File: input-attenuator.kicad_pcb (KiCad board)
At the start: 2 copper layers, 90.2 x 57.7 mm, 90 parts, among them J1 DC_INTF, J2 DC_INTF, J3 RX_1_RF, J4 RX_2_RF, J5 RF_IN, K1 EE2-5TNU-L, K2 EE2-5TNU-L, K3 EE2-5TNU-L, K4 EE2-5TNU-L, Q1 BC858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

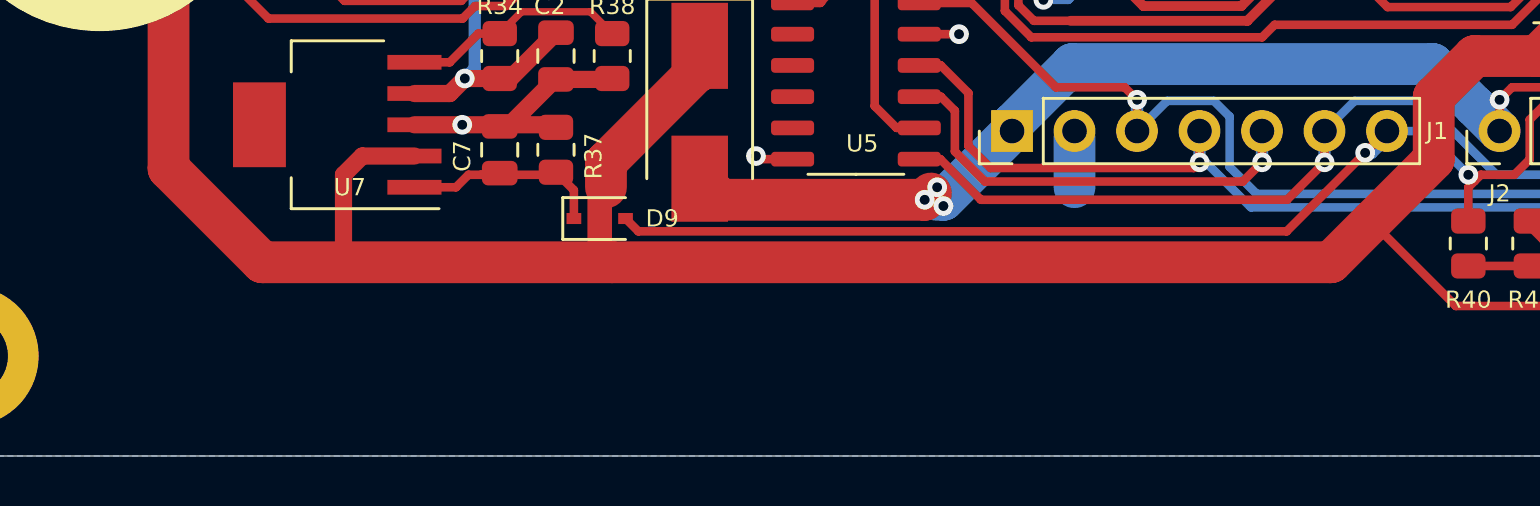
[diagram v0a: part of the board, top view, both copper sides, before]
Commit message: Updated layout with inrush resistor
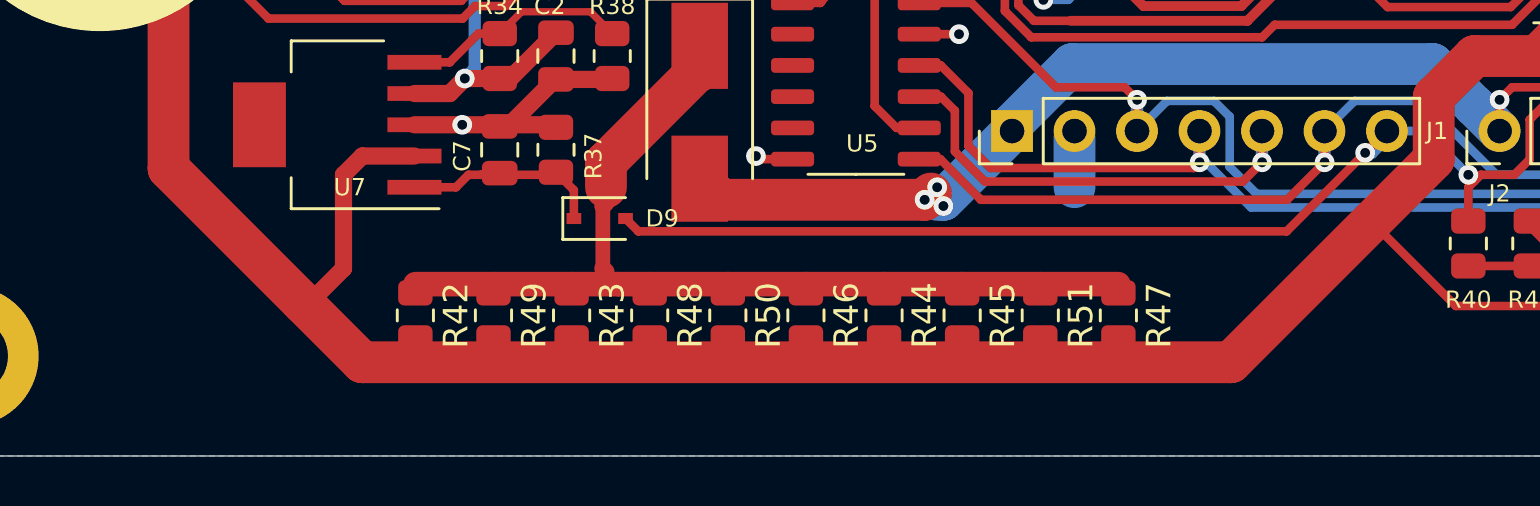
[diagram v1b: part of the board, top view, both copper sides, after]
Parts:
- added R42: 3K3, Resistor_SMD:R_0805_2012Metric, F.Cu at (85.7, 76.8)
- added R43: 3K3, Resistor_SMD:R_0805_2012Metric, F.Cu at (92.1, 76.8)
- added R44: 3K3, Resistor_SMD:R_0805_2012Metric, F.Cu at (104.8, 76.8)
- added R45: 3K3, Resistor_SMD:R_0805_2012Metric, F.Cu at (108.0, 76.8)
- added R46: 3K3, Resistor_SMD:R_0805_2012Metric, F.Cu at (101.6, 76.8)
- added R47: 3K3, Resistor_SMD:R_0805_2012Metric, F.Cu at (114.3, 76.8)
- added R48: 3K3, Resistor_SMD:R_0805_2012Metric, F.Cu at (95.2, 76.8)
- added R49: 3K3, Resistor_SMD:R_0805_2012Metric, F.Cu at (88.9, 76.8)
- added R50: 3K3, Resistor_SMD:R_0805_2012Metric, F.Cu at (98.4, 76.8)
- added R51: 3K3, Resistor_SMD:R_0805_2012Metric, F.Cu at (111.1, 76.8)
- J3: value RX_1_RF -> RX
- J4: value RX_2_RF -> ANT
- J5: value RF_IN -> TX
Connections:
- D10 pad 1: /Vin2 -> Net-(D10-Pad1)
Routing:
- net Net-(D10-Pad1): track 0.00 -> 39.6 mm
- net /Vin2: track 139.1 -> 135.0 mm

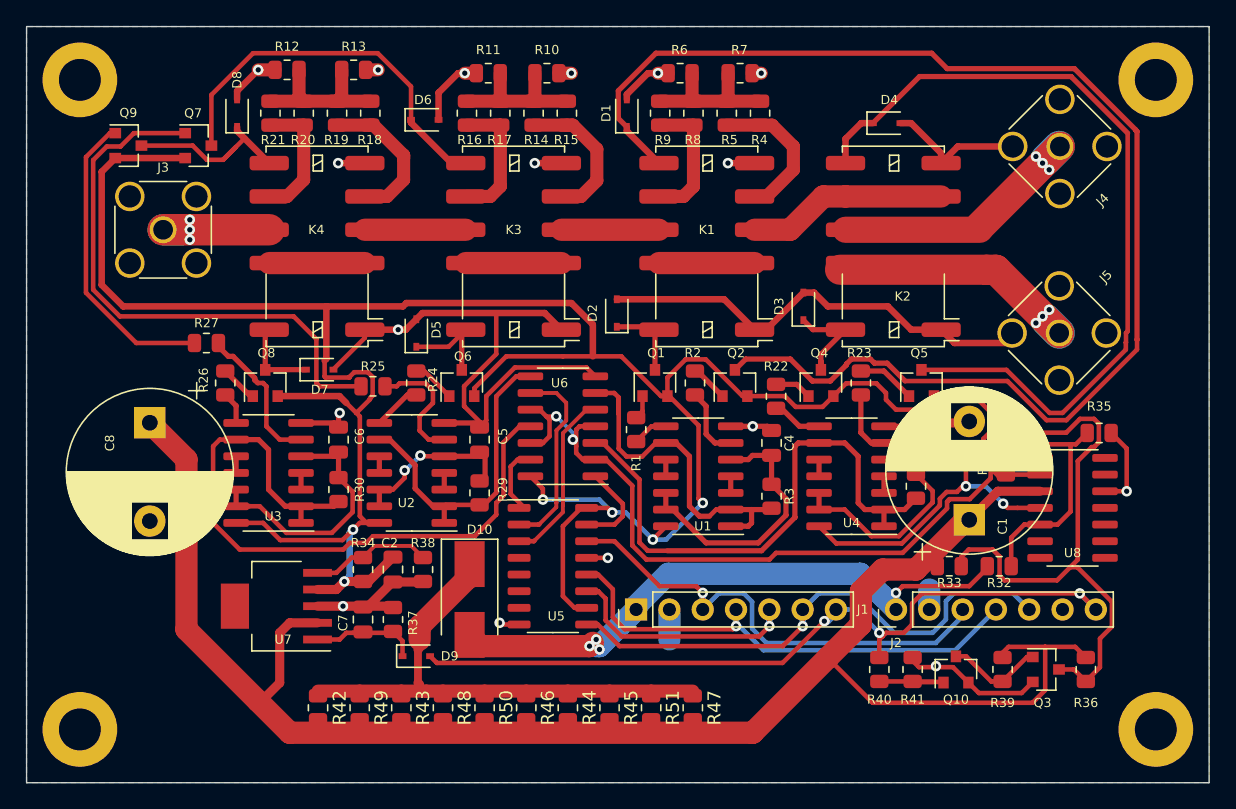
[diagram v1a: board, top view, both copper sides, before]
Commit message: Resized board and added auxilliary origin
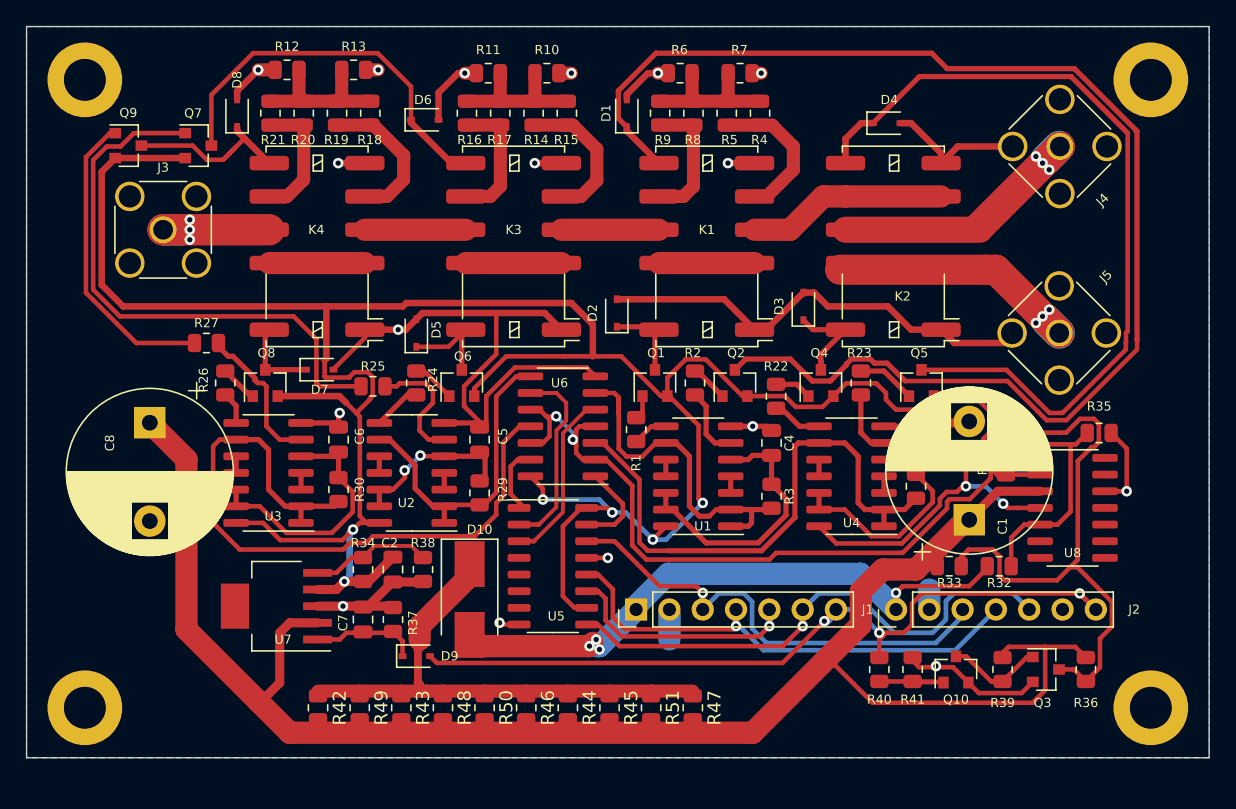
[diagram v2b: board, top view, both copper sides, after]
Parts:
- moved H1 1.69 mm to (149.2, 76.8)
- moved H3 1.69 mm to (67.9, 76.8)
- moved H2 0.38 mm to (149.2, 29.0)
- moved H4 0.38 mm to (67.9, 29.0)
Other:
- board size 90.2 x 57.7 mm -> 90.2 x 55.8 mm
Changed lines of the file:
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@@
     )
     (pad_to_mask_clearance 0)
+    (aux_axis_origin 63.5 80.645)
     (pcbplotparams
       (layerselection 0x00010fc_ffffffff)
@@
     (property "Sheetname" "")
     (attr through_hole)
-    (fp_text reference "J2" (at -2.54 0 180) (layer "F.SilkS")
+    (fp_text reference "J2" (at 0 18.161 180) (layer "F.SilkS")
       (effects (font (size 0.7 0.7) (thickness 0.12)))
     )
@@
   )
   (footprint "MountingHole:MountingHole_3.2mm_M3_ISO7380_Pad" (layer "F.Cu")
-    (at 149.606 28.956)
+    (at 149.225 28.956)
     (descr "Mounting Hole 3.2mm, M3, ISO7380")
     (tags "mounting hole 3.2mm m3 iso7380")
@@
     (fp_circle (center 0 0) (end 3.1 0) (layer "F.CrtYd") (width 0.05) (fill none))
     (pad "1" thru_hole circle (at 0 0) (locked) (size 5.7 5.7) (drill 3.2) (layers *.Cu *.Mask)
-      (net 11 "GND") (pinfunction "1") (pintype "input"))
+      (net 11 "GND") (pinfunction "1"))
   )
   (footprint "Diode_SMD:D_SOD-323" (layer "F.Cu")
@@
   )
   (footprint "MountingHole:MountingHole_3.2mm_M3_ISO7380_Pad" (layer "F.Cu")
-    (at 67.564 28.956)
+    (at 67.945 28.956)
     (descr "Mounting Hole 3.2mm, M3, ISO7380")
     (tags "mounting hole 3.2mm m3 iso7380")
@@
   )
   (footprint "MountingHole:MountingHole_3.2mm_M3_ISO7380_Pad" (layer "F.Cu")
-    (at 67.564 78.486)
+    (at 67.945 76.835)
     (descr "Mounting Hole 3.2mm, M3, ISO7380")
     (tags "mounting hole 3.2mm m3 iso7380")
@@
     (property "Sheetname" "")
     (attr through_hole)
-    (fp_text reference "J1" (at 0 17.277 180) (layer "F.SilkS")
+    (fp_text reference "J1" (at 0 17.658 180) (layer "F.SilkS")
       (effects (font (size 0.7 0.7) (thickness 0.12)))
     )
@@
   )
   (footprint "MountingHole:MountingHole_3.2mm_M3_ISO7380_Pad" (layer "F.Cu")
-    (at 149.606 78.486)
+    (at 149.225 76.835)
     (descr "Mounting Hole 3.2mm, M3, ISO7380")
     (tags "mounting hole 3.2mm m3 iso7380")
@@
     )
   )
-  (gr_rect (start 63.5 24.892) (end 153.67 82.55) (layer "Edge.Cuts") (width 0.05) (fill none))
+  (gr_rect (start 63.5 24.892) (end 153.67 80.645) (layer "Edge.Cuts") (width 0.05) (fill none))
   (segment (start 90.4 62.738) (end 89.425 62.738) (width 0.35) (layer "F.Cu") (net 1))
   (segment (start 106.207 61.595) (end 105.791 61.595) (width 0.35) (layer "F.Cu") (net 1))
@@
       (pts
         (xy 153.67 24.892)
-        (xy 153.67 82.55)
-        (xy 63.5 82.55)
+        (xy 153.67 80.645)
+        (xy 63.5 80.645)
         (xy 63.5 24.892)
       )
